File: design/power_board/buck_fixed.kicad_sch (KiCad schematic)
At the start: 9 parts

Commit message: Add files via upload
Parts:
- gave numbers to parts that had none: 8
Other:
- note added: "R7 is a chosen value from 1 kΩ–100 kΩ"
- note added: "Values for capacitors and inductors taken from https://www.ti.com/lit/ds/symlink/lv2862.pdf for VOUT = 12V"
- note added: "Voltage divider sets output voltage to 24V R6 = R7 ((VOUT/0.765)-1)"
- note added: "fsw = 2.1MHz"
- note removed: "A resistor between SET and GND sets the output voltage according to V = 0.75*221/R (kΩ) + 0.75"
- note removed: "Variable buck regulator. Most values taken from webench.ti.com for 17V out."
- note removed: "Voltage divider sets under-voltage lockout to 19.2V"
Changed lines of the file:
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@@
     (stroke (width 0) (type default))
   )
-  (text "Voltage divider sets\nunder-voltage lockout\nto 19.2V"
-    (at 97.79 77.47 0)
+  (text " fsw = 2.1MHz\n" (at 189.23 64.77 0)
     (effects (font (size 1.27 1.27)) (justify left bottom))
   )
-  (text "A resistor between SET and GND\nsets the output voltage according\nto V = 0.75*221/R (kΩ) + 0.75"
-    (at 176.53 127 0)
+  (text "Values for capacitors and inductors taken from \nhttps://www.ti.com/lit/ds/symlink/lv2862.pdf\nfor VOUT = 12V\n"
+    (at 130.81 63.5 0)
     (effects (font (size 1.27 1.27)) (justify left bottom))
   )
-  (text "Variable buck regulator. Most values taken from webench.ti.com for 17V out."
-    (at 168.91 64.77 0)
-    (effects (font (size 1.27 1.27)) (justify right bottom))
+  (text "R7 is a chosen value\nfrom 1 kΩ–100 kΩ" (at 148.59 123.19 0)
+    (effects (font (size 1.27 1.27)) (justify left bottom))
+  )
+  (text "Voltage divider sets\noutput voltage to 24V\nR6 = R7 ((VOUT/0.765)-1)"
+    (at 180.34 124.46 0)
+    (effects (font (size 1.27 1.27)) (justify left bottom))
   )
   (hierarchical_label "VOUT" (shape output) (at 206.375 95.25 0) (fields_autoplaced)
@@
   (symbol (lib_id "Device:C") (at 86.36 93.98 0) (unit 1)
     (in_bom yes) (on_board yes) (dnp no)
-    (property "Reference" "C?" (at 89.281 92.8116 0)
+    (property "Reference" "C1" (at 89.281 92.8116 0)
       (effects (font (size 1.27 1.27)) (justify left))
     )
@@
       (project "buck_fixed"
         (path "/5a149a99-7ef6-4309-ac70-ee1dc896f69a"
-          (reference "C?") (unit 1)
-        )
-      )
-      (project "power_board"
-        (path "/8a849c59-59c0-42e0-a511-c33c123656fd/00000000-0000-0000-0000-00006153da18"
           (reference "C1") (unit 1)
         )
       )
+      (project "power_board"
+        (path "/8a849c59-59c0-42e0-a511-c33c123656fd/00000000-0000-0000-0000-00006153da18"
+          (reference "C1") (unit 1)
+        )
+      )
     )
   )
   (symbol (lib_id "power:GND") (at 86.36 97.79 0) (unit 1)
     (in_bom yes) (on_board yes) (dnp no)
-    (property "Reference" "#PWR?" (at 86.36 104.14 0)
+    (property "Reference" "#PWR0105" (at 86.36 104.14 0)
       (effects (font (size 1.27 1.27)) hide)
     )
@@
       (project "buck_fixed"
         (path "/5a149a99-7ef6-4309-ac70-ee1dc896f69a"
-          (reference "#PWR?") (unit 1)
+          (reference "#PWR0105") (unit 1)
         )
       )
@@
   (symbol (lib_id "Device:C") (at 140.97 91.44 180) (unit 1)
     (in_bom yes) (on_board yes) (dnp no)
-    (property "Reference" "C?" (at 143.891 90.2716 0)
+    (property "Reference" "C2" (at 143.891 90.2716 0)
       (effects (font (size 1.27 1.27)) (justify right))
     )
@@
       (project "buck_fixed"
         (path "/5a149a99-7ef6-4309-ac70-ee1dc896f69a"
-          (reference "C?") (unit 1)
-        )
-      )
-      (project "power_board"
-        (path "/8a849c59-59c0-42e0-a511-c33c123656fd/00000000-0000-0000-0000-00006153da18"
           (reference "C2") (unit 1)
         )
       )
+      (project "power_board"
+        (path "/8a849c59-59c0-42e0-a511-c33c123656fd/00000000-0000-0000-0000-00006153da18"
+          (reference "C2") (unit 1)
+        )
+      )
     )
   )
   (symbol (lib_id "Device:D_Schottky") (at 147.955 99.06 270) (unit 1)
     (in_bom yes) (on_board yes) (dnp no)
-    (property "Reference" "D?" (at 149.987 97.8916 90)
+    (property "Reference" "D1" (at 149.987 97.8916 90)
       (effects (font (size 1.27 1.27)) (justify left))
     )
@@
       (project "buck_fixed"
         (path "/5a149a99-7ef6-4309-ac70-ee1dc896f69a"
-          (reference "D?") (unit 1)
-        )
-      )
-      (project "power_board"
-        (path "/8a849c59-59c0-42e0-a511-c33c123656fd/00000000-0000-0000-0000-00006153da18"
           (reference "D1") (unit 1)
         )
       )
+      (project "power_board"
+        (path "/8a849c59-59c0-42e0-a511-c33c123656fd/00000000-0000-0000-0000-00006153da18"
+          (reference "D1") (unit 1)
+        )
+      )
     )
   )
   (symbol (lib_id "Device:L") (at 161.29 95.25 90) (unit 1)
     (in_bom yes) (on_board yes) (dnp no)
-    (property "Reference" "L?" (at 161.29 90.424 90)
+    (property "Reference" "L1" (at 161.29 90.424 90)
       (effects (font (size 1.27 1.27)))
     )
@@
       (project "buck_fixed"
         (path "/5a149a99-7ef6-4309-ac70-ee1dc896f69a"
-          (reference "L?") (unit 1)
-        )
-      )
-      (project "power_board"
-        (path "/8a849c59-59c0-42e0-a511-c33c123656fd/00000000-0000-0000-0000-00006153da18"
           (reference "L1") (unit 1)
         )
       )
+      (project "power_board"
+        (path "/8a849c59-59c0-42e0-a511-c33c123656fd/00000000-0000-0000-0000-00006153da18"
+          (reference "L1") (unit 1)
+        )
+      )
     )
   )
   (symbol (lib_id "Device:R_US") (at 175.26 99.06 0) (unit 1)
     (in_bom yes) (on_board yes) (dnp no)
-    (property "Reference" "R?" (at 176.9872 97.8916 0)
+    (property "Reference" "R2" (at 176.9872 97.8916 0)
       (effects (font (size 1.27 1.27)) (justify left))
     )
@@
       (project "buck_fixed"
         (path "/5a149a99-7ef6-4309-ac70-ee1dc896f69a"
-          (reference "R?") (unit 1)
+          (reference "R2") (unit 1)
         )
       )
@@
   (symbol (lib_id "power:GND") (at 147.955 102.87 0) (unit 1)
     (in_bom yes) (on_board yes) (dnp no)
-    (property "Reference" "#PWR?" (at 147.955 109.22 0)
+    (property "Reference" "#PWR0102" (at 147.955 109.22 0)
       (effects (font (size 1.27 1.27)) hide)
     )
@@
       (project "buck_fixed"
         (path "/5a149a99-7ef6-4309-ac70-ee1dc896f69a"
-          (reference "#PWR?") (unit 1)
+          (reference "#PWR0102") (unit 1)
         )
       )
@@
       (project "buck_fixed"
         (path "/5a149a99-7ef6-4309-ac70-ee1dc896f69a"
-          (reference "#PWR?") (unit 1)
+          (reference "#PWR0103") (unit 1)
         )
       )
@@
   (symbol (lib_id "Buck:LV2862YDDCR") (at 102.87 87.63 0) (unit 1)
     (in_bom yes) (on_board yes) (dnp no) (fields_autoplaced)
-    (property "Reference" "U?" (at 120.65 78.74 0)
+    (property "Reference" "U1" (at 120.65 78.74 0)
       (effects (font (size 1.524 1.524)))
     )
@@
       (project "buck_fixed"
         (path "/5a149a99-7ef6-4309-ac70-ee1dc896f69a"
-          (reference "U?") (unit 1)
-        )
-      )
-      (project "power_board"
-        (path "/8a849c59-59c0-42e0-a511-c33c123656fd/00000000-0000-0000-0000-00006153da18"
           (reference "U1") (unit 1)
         )
       )
+      (project "power_board"
+        (path "/8a849c59-59c0-42e0-a511-c33c123656fd/00000000-0000-0000-0000-00006153da18"
+          (reference "U1") (unit 1)
+        )
+      )
     )
   )
   (symbol (lib_id "Device:R_US") (at 99.06 91.44 0) (unit 1)
     (in_bom yes) (on_board yes) (dnp no)
-    (property "Reference" "R?" (at 100.7872 90.2716 0)
+    (property "Reference" "R1" (at 100.7872 90.2716 0)
       (effects (font (size 1.27 1.27)) (justify left))
     )
@@
       (project "buck_fixed"
         (path "/5a149a99-7ef6-4309-ac70-ee1dc896f69a"
-          (reference "R?") (unit 1)
+          (reference "R1") (unit 1)
         )
       )
@@
   (symbol (lib_id "Device:R_US") (at 175.26 109.855 0) (unit 1)
     (in_bom yes) (on_board yes) (dnp no)
-    (property "Reference" "R?" (at 176.9872 108.6866 0)
+    (property "Reference" "R3" (at 176.9872 108.6866 0)
       (effects (font (size 1.27 1.27)) (justify left))
     )
@@
       (project "buck_fixed"
         (path "/5a149a99-7ef6-4309-ac70-ee1dc896f69a"
-          (reference "R?") (unit 1)
+          (reference "R3") (unit 1)
         )
       )
@@
   (symbol (lib_id "power:GND") (at 175.26 113.665 0) (unit 1)
     (in_bom yes) (on_board yes) (dnp no)
-    (property "Reference" "#PWR?" (at 175.26 120.015 0)
+    (property "Reference" "#PWR0104" (at 175.26 120.015 0)
       (effects (font (size 1.27 1.27)) hide)
     )
@@
       (project "buck_fixed"
         (path "/5a149a99-7ef6-4309-ac70-ee1dc896f69a"
-          (reference "#PWR?") (unit 1)
+          (reference "#PWR0104") (unit 1)
         )
       )
@@
   (symbol (lib_id "power:GND") (at 138.43 111.125 0) (unit 1)
     (in_bom yes) (on_board yes) (dnp no)
-    (property "Reference" "#PWR?" (at 138.43 117.475 0)
+    (property "Reference" "#PWR0101" (at 138.43 117.475 0)
       (effects (font (size 1.27 1.27)) hide)
     )
@@
       (project "buck_fixed"
         (path "/5a149a99-7ef6-4309-ac70-ee1dc896f69a"
-          (reference "#PWR?") (unit 1)
+          (reference "#PWR0101") (unit 1)
         )
       )
@@
       (project "buck_fixed"
         (path "/5a149a99-7ef6-4309-ac70-ee1dc896f69a"
-          (reference "COUT?") (unit 1)
-        )
-      )
-      (project "power_board"
-        (path "/8a849c59-59c0-42e0-a511-c33c123656fd/00000000-0000-0000-0000-00006153da18"
           (reference "COUT1") (unit 1)
         )
       )
-    )
+      (project "power_board"
+        (path "/8a849c59-59c0-42e0-a511-c33c123656fd/00000000-0000-0000-0000-00006153da18"
+          (reference "COUT1") (unit 1)
+        )
+      )
+    )
+  )
+  (sheet_instances
+    (path "/" (page "1"))
   )
 )

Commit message: Changed footprint Changed footprint path changed footprint Edit Edit Edit
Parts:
- U1: footprint footprints:DDC0006A-IPC_A -> Package_TO_SOT_SMD:TSOT-23-6_HandSoldering
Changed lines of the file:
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@@
       (effects (font (size 1.524 1.524)))
     )
-    (property "Footprint" "footprints:DDC0006A-IPC_A" (at 82.55 90.17 0)
+    (property "Footprint" "Package_TO_SOT_SMD:TSOT-23-6_HandSoldering" (at 82.55 90.17 0)
       (effects (font (size 1.27 1.27) italic) hide)
     )

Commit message: Edited calculations
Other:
- note added: "Resistor values for R6 = 10k: R7 sets the voltage output for 22V out (20V out of LDO) R9 = 10(22/0.765 - 1) R9 = 277.58k for 14V (12V out of LDO): R9 = 10(14/0.765 - 1) R9 = 173k for 12V (10V out of LDO): R9 = 10(12/0.765 - 1) R9 = 146.86k for 7V(5V out of LDO): R9 = 10(7/0.765 - 1) R9 = 81.50k Both 1%"
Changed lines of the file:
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@@
+    (effects (font (size 1.27 1.27)) (justify left bottom))
+  )
+  (text "Resistor values for R6 = 10k:\nR7 sets the voltage output\nfor 22V out (20V out of LDO)\n	R9 = 10(22/0.765 - 1)\n	R9 = 277.58k\n\nfor 14V (12V out of LDO):\n  R9 = 10(14/0.765 - 1)\n  R9 = 173k\n\nfor 12V (10V out of LDO):\n  R9 = 10(12/0.765 - 1)\n  R9 = 146.86k\n\nfor 7V(5V out of LDO):\n  R9 = 10(7/0.765 - 1)\n  R9 = 81.50k\n\nBoth 1%"
+    (at 222.25 111.76 0)
     (effects (font (size 1.27 1.27)) (justify left bottom))
   )

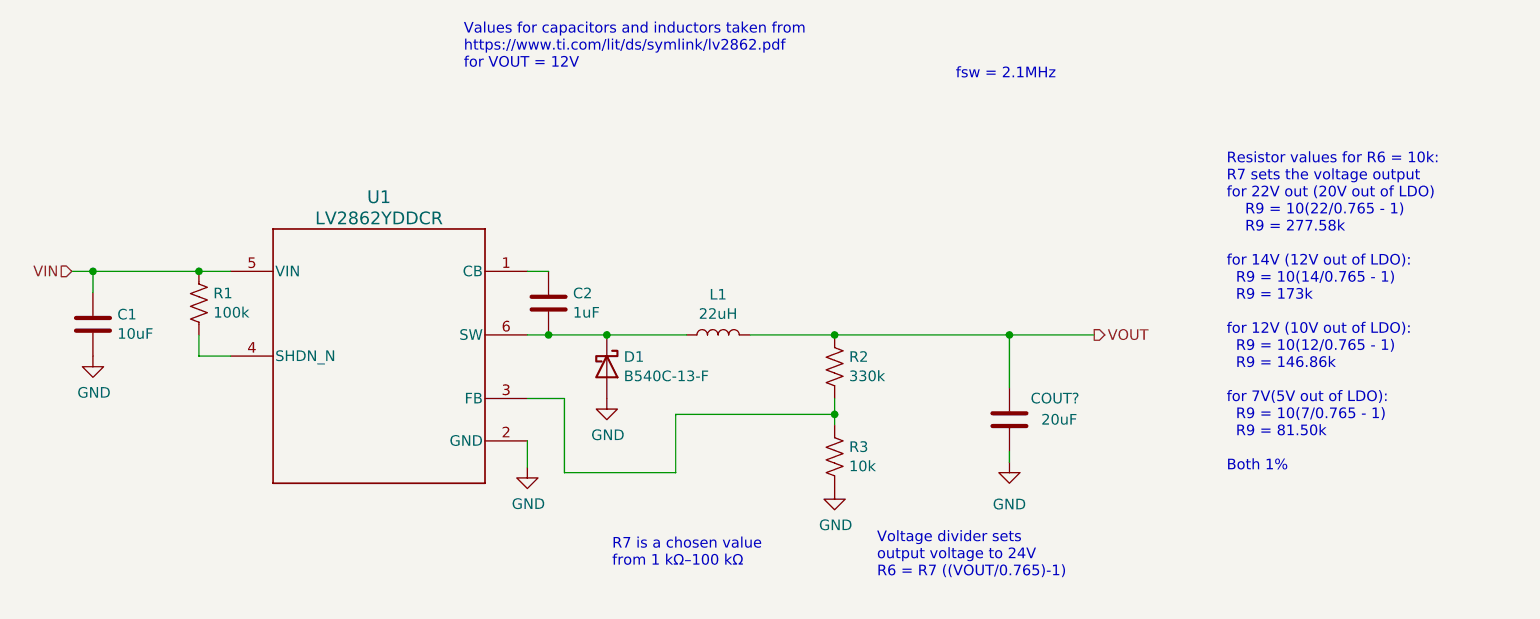
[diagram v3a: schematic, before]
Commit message: Added capacitor, switched input to right side`
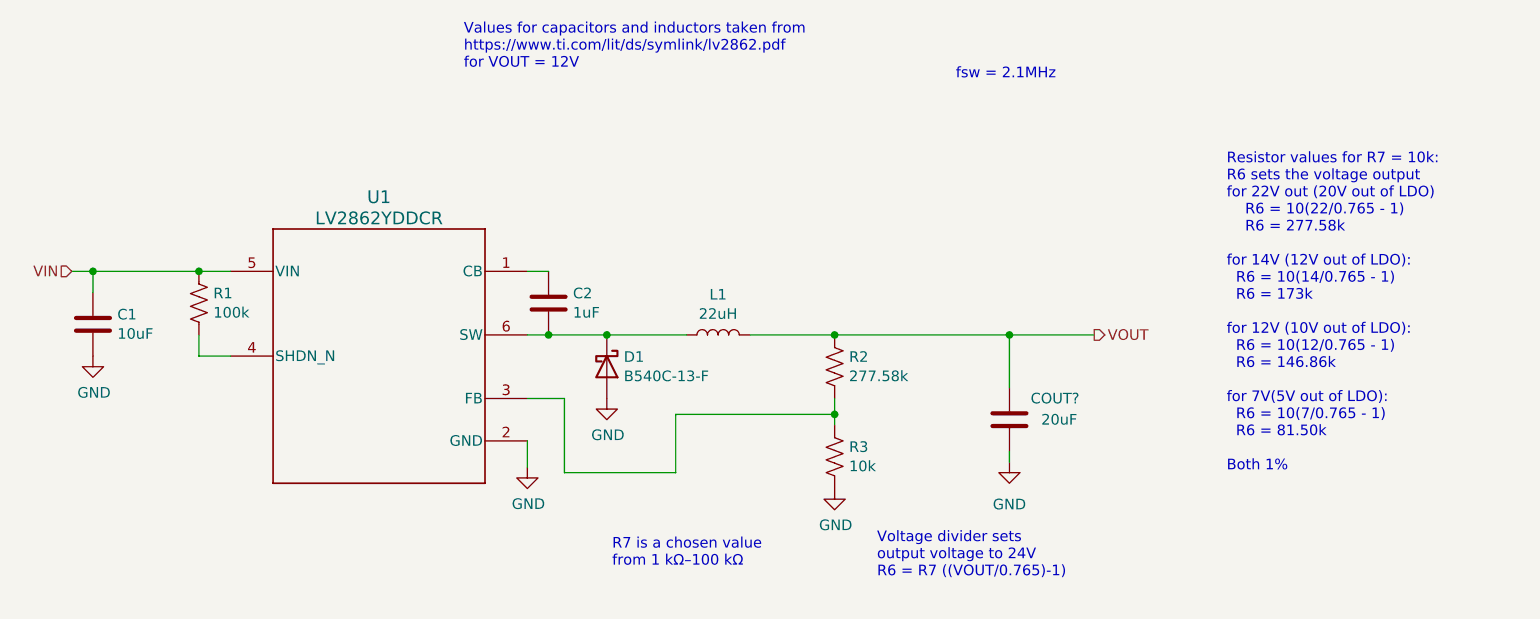
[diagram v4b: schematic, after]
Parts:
- R2: value 330k -> 277.58k
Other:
- note added: "Resistor values for R7 = 10k: R6 sets the voltage output for 22V out (20V out of LDO) R6 = 10(22/0.765 - 1) R6 = 277.58k for 14V (12V out of LDO): R6 = 10(14/0.765 - 1) R6 = 173k for 12V (10V out of LDO): R6 = 10(12/0.765 - 1) R6 = 146.86k for 7V(5V out of LDO): R6 = 10(7/0.765 - 1) R6 = 81.50k Both 1%"
- note removed: "Resistor values for R6 = 10k: R7 sets the voltage output for 22V out (20V out of LDO) R9 = 10(22/0.765 - 1) R9 = 277.58k for 14V (12V out of LDO): R9 = 10(14/0.765 - 1) R9 = 173k for 12V (10V out of LDO): R9 = 10(12/0.765 - 1) R9 = 146.86k for 7V(5V out of LDO): R9 = 10(7/0.765 - 1) R9 = 81.50k Both 1%"
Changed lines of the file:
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@@
     (effects (font (size 1.27 1.27)) (justify left bottom))
   )
-  (text "Resistor values for R6 = 10k:\nR7 sets the voltage output\nfor 22V out (20V out of LDO)\n	R9 = 10(22/0.765 - 1)\n	R9 = 277.58k\n\nfor 14V (12V out of LDO):\n  R9 = 10(14/0.765 - 1)\n  R9 = 173k\n\nfor 12V (10V out of LDO):\n  R9 = 10(12/0.765 - 1)\n  R9 = 146.86k\n\nfor 7V(5V out of LDO):\n  R9 = 10(7/0.765 - 1)\n  R9 = 81.50k\n\nBoth 1%"
+  (text "Resistor values for R7 = 10k:\nR6 sets the voltage output\nfor 22V out (20V out of LDO)\n	R6 = 10(22/0.765 - 1)\n	R6 = 277.58k\n\nfor 14V (12V out of LDO):\n  R6 = 10(14/0.765 - 1)\n  R6 = 173k\n\nfor 12V (10V out of LDO):\n  R6 = 10(12/0.765 - 1)\n  R6 = 146.86k\n\nfor 7V(5V out of LDO):\n  R6 = 10(7/0.765 - 1)\n  R6 = 81.50k\n\nBoth 1%"
     (at 222.25 111.76 0)
     (effects (font (size 1.27 1.27)) (justify left bottom))
@@
       (effects (font (size 1.27 1.27)) (justify left))
     )
-    (property "Value" "330k" (at 176.9872 100.203 0)
+    (property "Value" "277.58k" (at 176.9872 100.203 0)
       (effects (font (size 1.27 1.27)) (justify left))
     )

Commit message: i
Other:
- note added: "Values for capacitors and inductors taken from https://www.ti.com/lit/ds/symlink/lv2862.pdf"
- note removed: "Values for capacitors and inductors taken from https://www.ti.com/lit/ds/symlink/lv2862.pdf for VOUT = 12V"
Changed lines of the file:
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@@
     (stroke (width 0) (type default))
   )
-  (text " fsw = 2.1MHz\n" (at 189.23 64.77 0)
+  (text " fsw = 2.1MHz\n" (at 185.42 83.82 0)
     (effects (font (size 1.27 1.27)) (justify left bottom))
   )
-  (text "Values for capacitors and inductors taken from \nhttps://www.ti.com/lit/ds/symlink/lv2862.pdf\nfor VOUT = 12V\n"
-    (at 130.81 63.5 0)
+  (text "Values for capacitors and inductors taken from \nhttps://www.ti.com/lit/ds/symlink/lv2862.pdf\n"
+    (at 134.62 73.66 0)
     (effects (font (size 1.27 1.27)) (justify left bottom))
   )
@@
   )
   (text "Resistor values for R7 = 10k:\nR6 sets the voltage output\nfor 22V out (20V out of LDO)\n	R6 = 10(22/0.765 - 1)\n	R6 = 277.58k\n\nfor 14V (12V out of LDO):\n  R6 = 10(14/0.765 - 1)\n  R6 = 173k\n\nfor 12V (10V out of LDO):\n  R6 = 10(12/0.765 - 1)\n  R6 = 146.86k\n\nfor 7V(5V out of LDO):\n  R6 = 10(7/0.765 - 1)\n  R6 = 81.50k\n\nBoth 1%"
-    (at 222.25 111.76 0)
+    (at 214.63 109.22 0)
     (effects (font (size 1.27 1.27)) (justify left bottom))
   )
